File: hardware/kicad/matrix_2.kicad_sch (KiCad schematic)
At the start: 142 parts, among them U6 IS31FL3741A

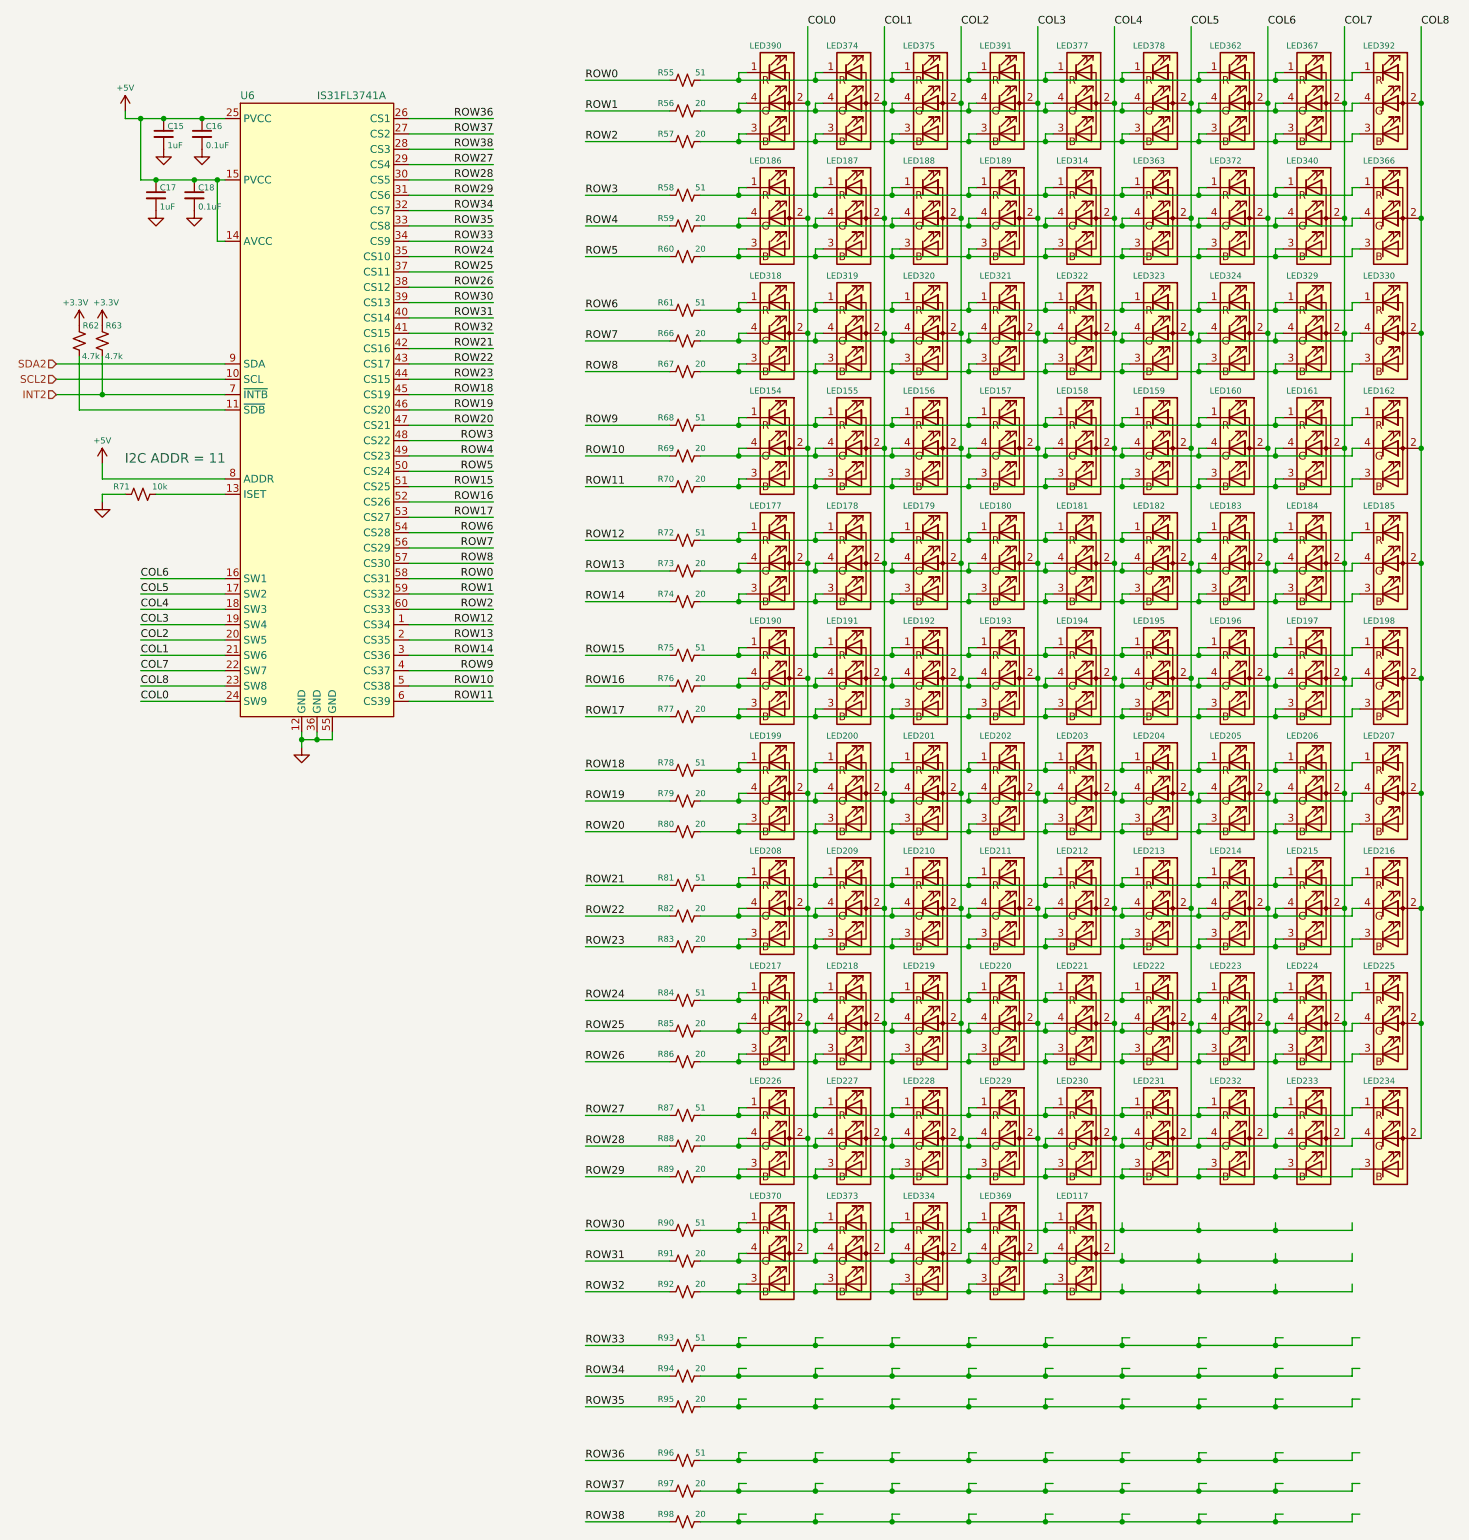
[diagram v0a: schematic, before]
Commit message: update new led numbers
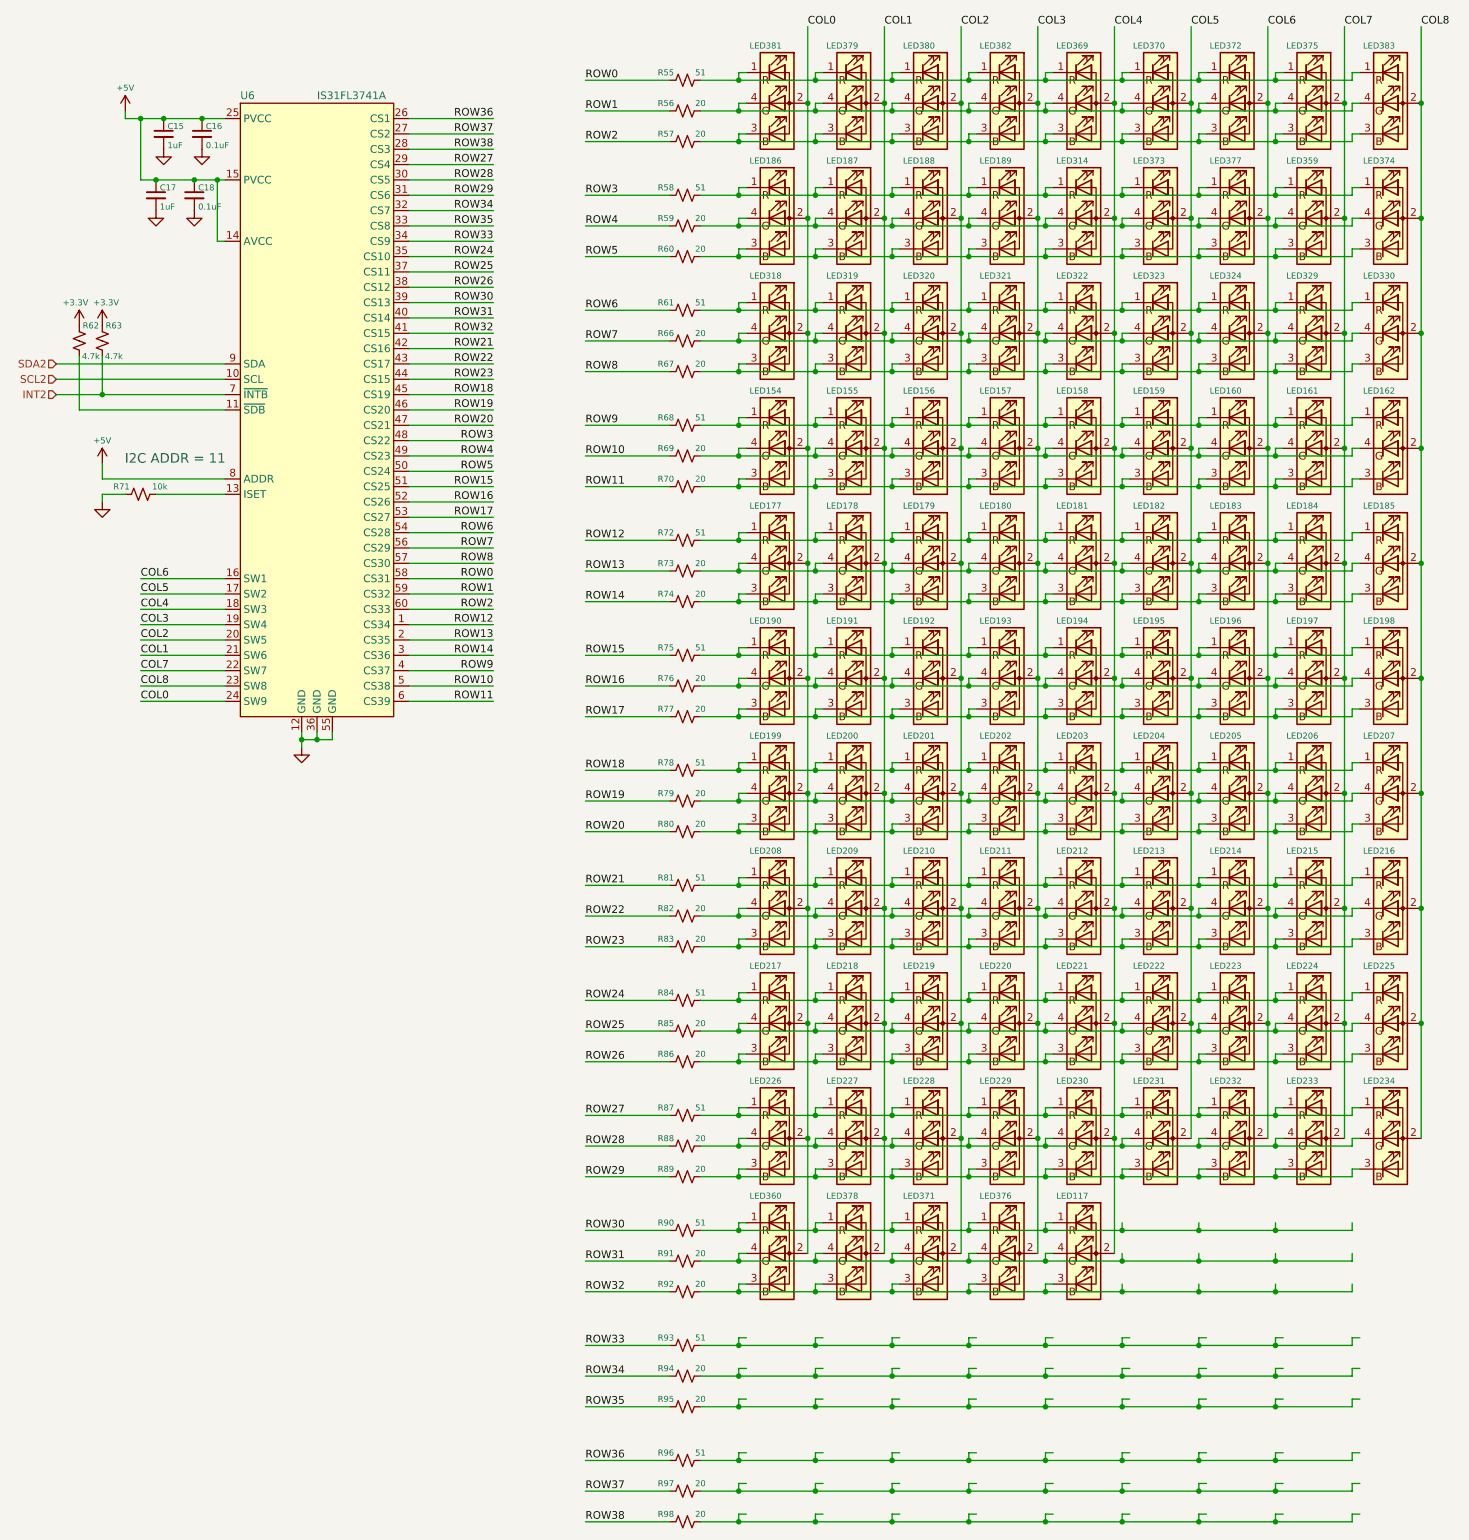
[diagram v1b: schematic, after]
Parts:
- renumbered LED340 to LED359, LED370 to LED360, LED377 to LED369, LED378 to LED370, LED334 to LED371, LED362 to LED372, LED363 to LED373, LED366 to LED374, LED367 to LED375, LED369 to LED376, LED372 to LED377, LED373 to LED378, LED374 to LED379, LED375 to LED380, LED390 to LED381, LED391 to LED382, LED392 to LED383
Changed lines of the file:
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@@
 		(on_board yes)
 		(dnp no)
-		(property "Reference" "LED369"
+		(property "Reference" "LED376"
 			(at 188.595 216.535 0)
 			(effects
@@
 			(project "traffic_paradise"
 				(path "/911505fc-874d-4338-908e-12054bdd5112/a4b8a9ee-0dc2-43fe-8aa1-46a166ad2321"
-					(reference "LED369")
+					(reference "LED376")
 					(unit 1)
 				)
@@
 		(on_board yes)
 		(dnp no)
-		(property "Reference" "LED375"
+		(property "Reference" "LED380"
 			(at 175.895 26.035 0)
 			(effects
@@
 			(project "traffic_paradise"
 				(path "/911505fc-874d-4338-908e-12054bdd5112/a4b8a9ee-0dc2-43fe-8aa1-46a166ad2321"
-					(reference "LED375")
+					(reference "LED380")
 					(unit 1)
 				)
@@
 		(on_board yes)
 		(dnp no)
-		(property "Reference" "LED392"
+		(property "Reference" "LED383"
 			(at 252.095 26.035 0)
 			(effects
@@
 			(project "traffic_paradise"
 				(path "/911505fc-874d-4338-908e-12054bdd5112/a4b8a9ee-0dc2-43fe-8aa1-46a166ad2321"
-					(reference "LED392")
+					(reference "LED383")
 					(unit 1)
 				)
@@
 		(on_board yes)
 		(dnp no)
-		(property "Reference" "LED372"
+		(property "Reference" "LED377"
 			(at 226.695 45.085 0)
 			(effects
@@
 			(project "traffic_paradise"
 				(path "/911505fc-874d-4338-908e-12054bdd5112/a4b8a9ee-0dc2-43fe-8aa1-46a166ad2321"
-					(reference "LED372")
+					(reference "LED377")
 					(unit 1)
 				)
@@
 		(on_board yes)
 		(dnp no)
-		(property "Reference" "LED373"
+		(property "Reference" "LED378"
 			(at 163.195 216.535 0)
 			(effects
@@
 			(project "traffic_paradise"
 				(path "/911505fc-874d-4338-908e-12054bdd5112/a4b8a9ee-0dc2-43fe-8aa1-46a166ad2321"
-					(reference "LED373")
+					(reference "LED378")
 					(unit 1)
 				)
@@
 		(on_board yes)
 		(dnp no)
-		(property "Reference" "LED377"
+		(property "Reference" "LED369"
 			(at 201.295 26.035 0)
 			(effects
@@
 			(project "traffic_paradise"
 				(path "/911505fc-874d-4338-908e-12054bdd5112/a4b8a9ee-0dc2-43fe-8aa1-46a166ad2321"
-					(reference "LED377")
+					(reference "LED369")
 					(unit 1)
 				)
@@
 		(on_board yes)
 		(dnp no)
-		(property "Reference" "LED362"
+		(property "Reference" "LED372"
 			(at 226.695 26.035 0)
 			(effects
@@
 			(project "traffic_paradise"
 				(path "/911505fc-874d-4338-908e-12054bdd5112/a4b8a9ee-0dc2-43fe-8aa1-46a166ad2321"
-					(reference "LED362")
+					(reference "LED372")
 					(unit 1)
 				)
@@
 		(on_board yes)
 		(dnp no)
-		(property "Reference" "LED391"
+		(property "Reference" "LED382"
 			(at 188.595 26.035 0)
 			(effects
@@
 			(project "traffic_paradise"
 				(path "/911505fc-874d-4338-908e-12054bdd5112/a4b8a9ee-0dc2-43fe-8aa1-46a166ad2321"
-					(reference "LED391")
+					(reference "LED382")
 					(unit 1)
 				)
@@
 		(on_board yes)
 		(dnp no)
-		(property "Reference" "LED374"
+		(property "Reference" "LED379"
 			(at 163.195 26.035 0)
 			(effects
@@
 			(project "traffic_paradise"
 				(path "/911505fc-874d-4338-908e-12054bdd5112/a4b8a9ee-0dc2-43fe-8aa1-46a166ad2321"
-					(reference "LED374")
+					(reference "LED379")
 					(unit 1)
 				)
@@
 		(on_board yes)
 		(dnp no)
-		(property "Reference" "LED363"
+		(property "Reference" "LED373"
 			(at 213.995 45.085 0)
 			(effects
@@
 			(project "traffic_paradise"
 				(path "/911505fc-874d-4338-908e-12054bdd5112/a4b8a9ee-0dc2-43fe-8aa1-46a166ad2321"
-					(reference "LED363")
+					(reference "LED373")
 					(unit 1)
 				)
@@
 		(on_board yes)
 		(dnp no)
-		(property "Reference" "LED334"
+		(property "Reference" "LED371"
 			(at 175.895 216.535 0)
 			(effects
@@
 			(project "traffic_paradise"
 				(path "/911505fc-874d-4338-908e-12054bdd5112/a4b8a9ee-0dc2-43fe-8aa1-46a166ad2321"
-					(reference "LED334")
+					(reference "LED371")
 					(unit 1)
 				)
@@
 		(on_board yes)
 		(dnp no)
-		(property "Reference" "LED370"
+		(property "Reference" "LED360"
 			(at 150.495 216.535 0)
 			(effects
@@
 			(project "traffic_paradise"
 				(path "/911505fc-874d-4338-908e-12054bdd5112/a4b8a9ee-0dc2-43fe-8aa1-46a166ad2321"
-					(reference "LED370")
+					(reference "LED360")
 					(unit 1)
 				)
@@
 		(on_board yes)
 		(dnp no)
-		(property "Reference" "LED367"
+		(property "Reference" "LED375"
 			(at 239.395 26.035 0)
 			(effects
@@
 			(project "traffic_paradise"
 				(path "/911505fc-874d-4338-908e-12054bdd5112/a4b8a9ee-0dc2-43fe-8aa1-46a166ad2321"
-					(reference "LED367")
+					(reference "LED375")
 					(unit 1)
 				)
@@
 		(on_board yes)
 		(dnp no)
-		(property "Reference" "LED366"
+		(property "Reference" "LED374"
 			(at 252.095 45.085 0)
 			(effects
@@
 			(project "traffic_paradise"
 				(path "/911505fc-874d-4338-908e-12054bdd5112/a4b8a9ee-0dc2-43fe-8aa1-46a166ad2321"
-					(reference "LED366")
+					(reference "LED374")
 					(unit 1)
 				)
@@
 		(on_board yes)
 		(dnp no)
-		(property "Reference" "LED340"
+		(property "Reference" "LED359"
 			(at 239.395 45.085 0)
 			(effects
@@
 			(project "traffic_paradise"
 				(path "/911505fc-874d-4338-908e-12054bdd5112/a4b8a9ee-0dc2-43fe-8aa1-46a166ad2321"
-					(reference "LED340")
+					(reference "LED359")
 					(unit 1)
 				)
@@
 		(on_board yes)
 		(dnp no)
-		(property "Reference" "LED378"
+		(property "Reference" "LED370"
 			(at 213.995 26.035 0)
 			(effects
@@
 			(project "traffic_paradise"
 				(path "/911505fc-874d-4338-908e-12054bdd5112/a4b8a9ee-0dc2-43fe-8aa1-46a166ad2321"
-					(reference "LED378")
+					(reference "LED370")
 					(unit 1)
 				)
@@
 		(on_board yes)
 		(dnp no)
-		(property "Reference" "LED390"
+		(property "Reference" "LED381"
 			(at 150.495 26.035 0)
 			(effects
@@
 			(project "traffic_paradise"
 				(path "/911505fc-874d-4338-908e-12054bdd5112/a4b8a9ee-0dc2-43fe-8aa1-46a166ad2321"
-					(reference "LED390")
+					(reference "LED381")
 					(unit 1)
 				)
